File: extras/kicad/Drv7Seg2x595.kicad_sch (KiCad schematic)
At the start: 33 parts, among them IC1 74HC595, IC2 74HC595, J1 INTERFACE, J2 PWR_LED_JMP, Q1 MMBT3904, Q2 MMBT3904, Q3 MMBT3904, Q4 MMBT3904

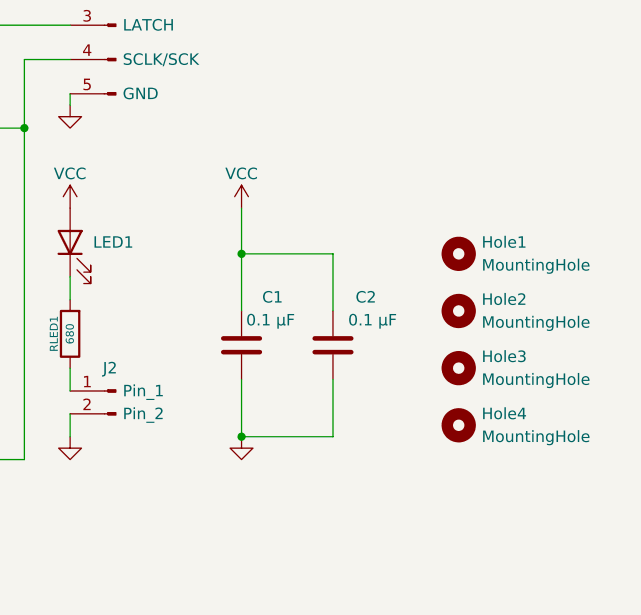
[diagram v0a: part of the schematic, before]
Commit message: Restyle interface header labels + move mounting holes symbols on schematic a bit.
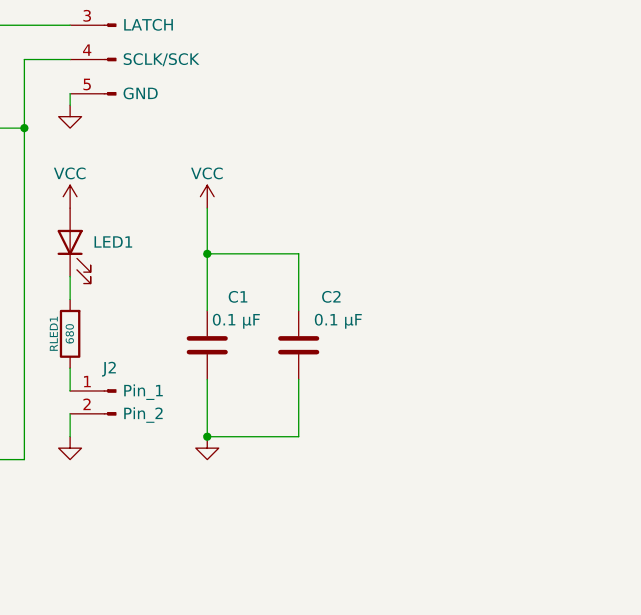
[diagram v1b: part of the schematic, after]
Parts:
- removed Hole1, Hole2, Hole3, Hole4: MountingHole, MountingHole:MountingHole_3mm, symbol Mechanical:MountingHole
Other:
- moved on the sheet: C1, C2

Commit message: Return mounting holes (deleted them accidentally while taking a screenshot).
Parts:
- added Hole1, Hole2, Hole3, Hole4: MountingHole, MountingHole:MountingHole_3mm, symbol Mechanical:MountingHole
